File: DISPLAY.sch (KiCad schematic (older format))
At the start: 31 parts, among them Q301 BC849

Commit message: Prepare Display change
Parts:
- removed C310, C311: 100n, Capacitors_SMD:C_0603, symbol C_Small
- removed Q301: BC849, TO_SOT_Packages_SMD:SOT-23, symbol BC849
- removed R301: 4k7, Resistors_SMD:R_0603, symbol R
- removed R302, R303: 0, Resistors_SMD:R_0603, symbol R
- removed R304: 22, Resistors_SMD:R_0603, symbol R
- removed R305, R306, R307, R308, R309: 100, Resistors_SMD:R_0603, symbol R
- removed TP303, TP304, TP305, TP306, TP307, TP308, TP309, TP310, TP311, TP312, TP313, TP314, TP315: TP, buttons:TP, symbol TP
- added P?: SEPS525, symbol CONN_01X35
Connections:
- net labels removed: +3V3, +4V, AO, AO_IN, BL_ON, CS, CS_IN, LED+, LED-, RST, RST_IN, SCK, SCK_IN, SDA, SDA_IN
- wire segments 35 -> 9
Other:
- note added: "160x128 pixel \nOLED display"
- note added: "NC\nVSDH\nVDDH\nVSSH\nIREF\nOSCA2\nOSCA1\nVDDIO\nVSYNCO\nVSYNC\nHSYNC\nDOTCLK\nENABLE\nCPU\nPS\nD17\nD16\nD15\nD14\nD13\nD12\nD11\nD10\nD9\nRS\nCSB\nRDB\nWRB\nRESETB\nVSS\nVDD\nVSSH\nVSDH\nNC"
- note removed: "Constant current: 18mA"
- note removed: "ev.R"
- moved on the sheet: C308, C309, L301, L302, TP301, TP302

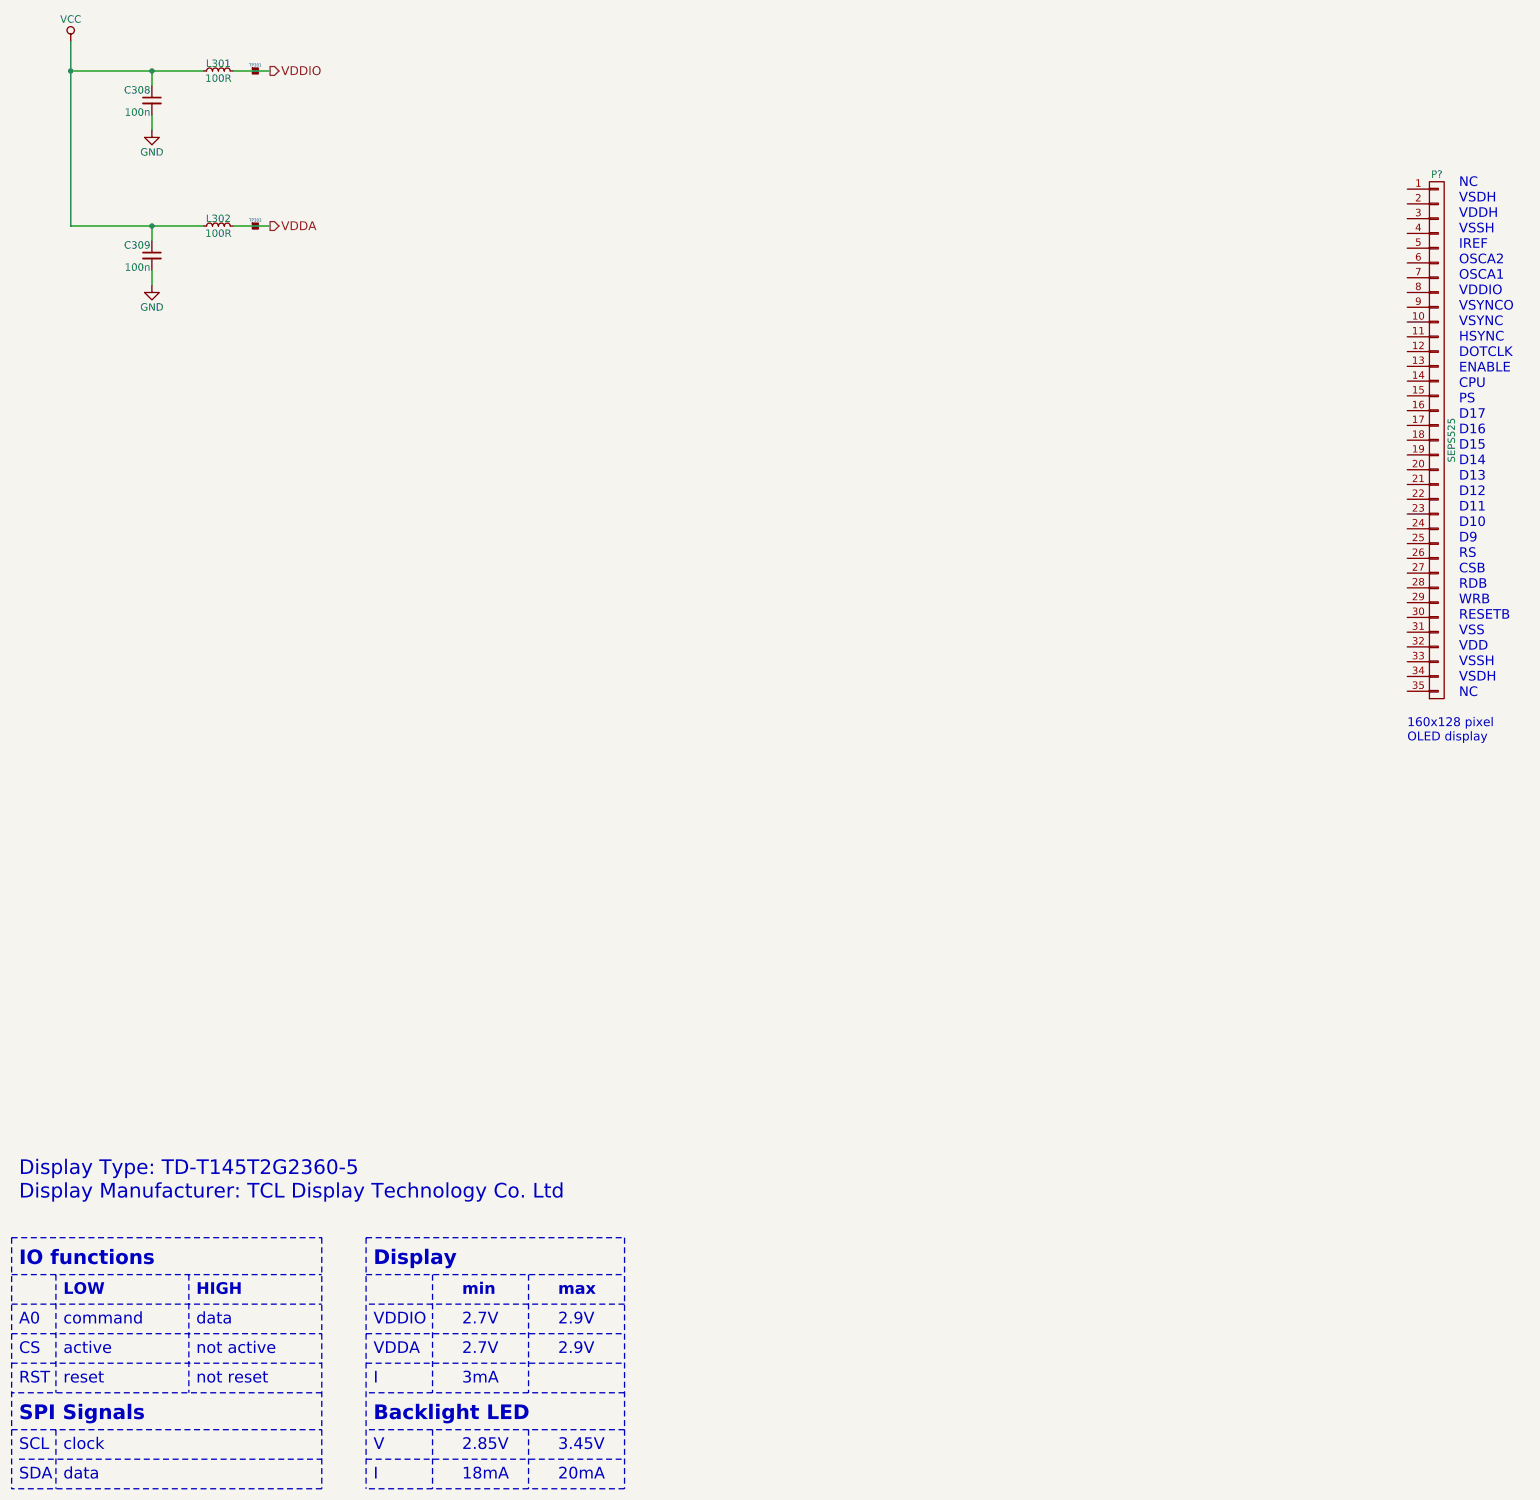
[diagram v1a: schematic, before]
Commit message: Added Interface for OLED display
Added Booster for 4V -> 15V
Added bus for display data
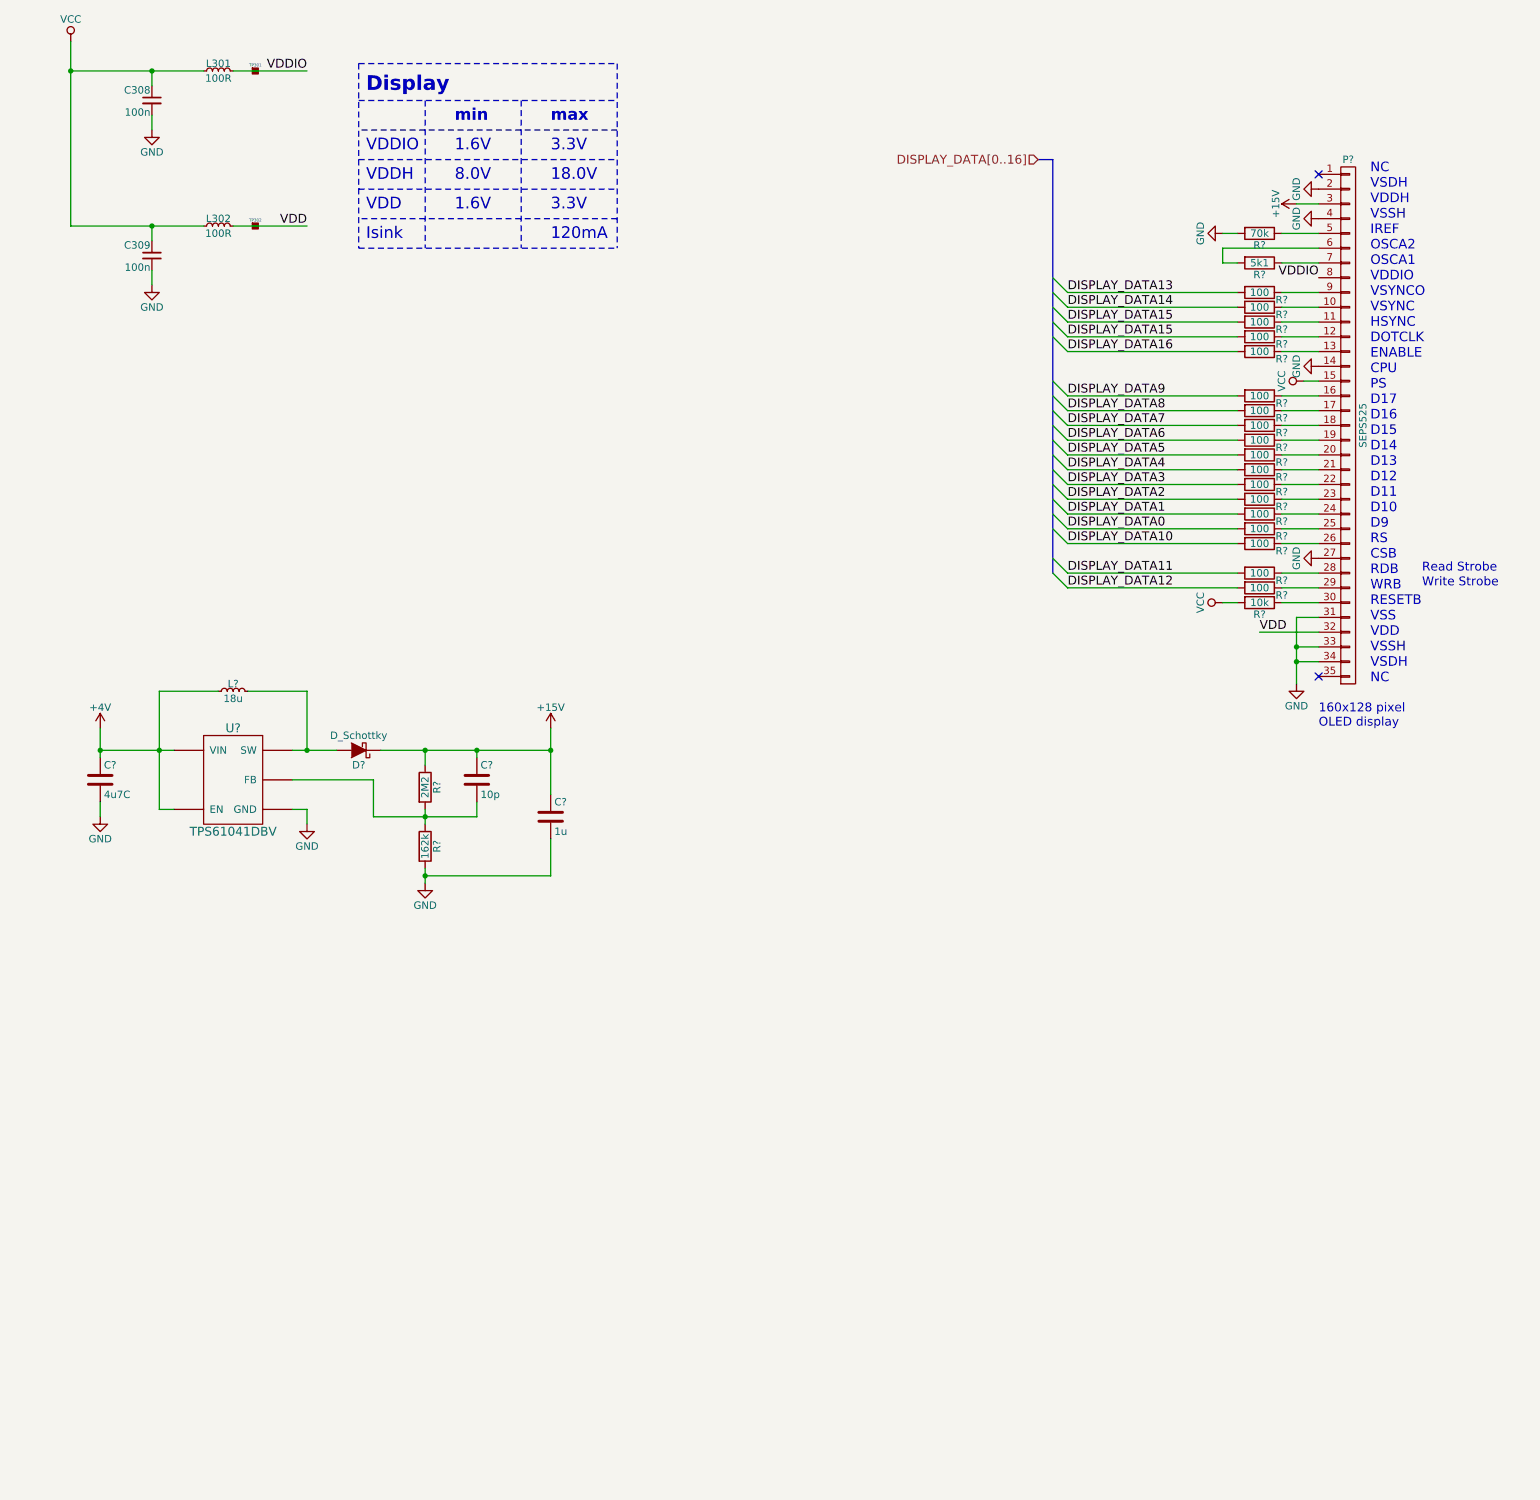
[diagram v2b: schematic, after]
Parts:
- added C?: 4u7C, symbol C
- added C?: 10p, symbol C
- added C?: 1u, symbol C
- added D?: D_Schottky, symbol D_Schottky
- added L?: 18u, Resistors_SMD:R_0603, symbol L_Small
- added R?: 10k, symbol R
- added R?: 5k1, symbol R
- added R?: 70k, symbol R
- added R?: 2M2, symbol R
- added R?: 162k, symbol R
- added R? (x18): 100, symbol R
- added U?: TPS61041DBV, symbol TPS61041DBV
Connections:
- net VDDA is gone; now on net VDD: L302.1
- net GND: now also P?.14 (P14), P?.2 (P2), P?.27 (P27), P?.31 (P31), P?.33 (P33), P?.34 (P34), P?.4 (P4), C?.2, C?.2, R?.2, R?.2, U?.~ (VIN)
- net VCC: now also P?.15 (P15), R?.2
- net VDDIO: now also P?.8 (P8)
- net at P?.10 (P10): now also R?.1
- net at P?.11 (P11): now also R?.1
- net at P?.12 (P12): now also R?.1
- net at P?.13 (P13): now also R?.1
- net at P?.16 (P16): now also R?.1
- net at P?.17 (P17): now also R?.1
- net at P?.18 (P18): now also R?.1
- net at P?.19 (P19): now also R?.1
- net at P?.20 (P20): now also R?.1
- net at P?.21 (P21): now also R?.1
- net at P?.22 (P22): now also R?.1
- net at P?.23 (P23): now also R?.1
- net at P?.24 (P24): now also R?.1
- net at P?.25 (P25): now also R?.1
- net at P?.26 (P26): now also R?.1
- net at P?.28 (P28): now also R?.1
- net at P?.29 (P29): now also R?.1
- net +15V: now reaches P?.3 (P3)
- net +15V: now also C?.1, C?.1, D?.1 (K), R?.1
- net at P?.30 (P30): now also R?.1
- net VDD: now reaches P?.32 (P32)
- net at P?.5 (P5): now also R?.1
- net at P?.6 (P6): now also R?.2
- net at P?.7 (P7): now also R?.1
- net at P?.9 (P9): now also R?.1
- new net: D?.2 (A), L?.1, U?.~ (VIN)
- new net: C?.2, R?.1, R?.2, U?.~ (VIN)
- new net +4V: C?.1, L?.2, U?.~ (VIN)
- new net DISPLAY_DATA0: R?.2
- new net DISPLAY_DATA1: R?.2
- new net DISPLAY_DATA10: R?.2
- new net DISPLAY_DATA11: R?.2
- new net DISPLAY_DATA12: R?.2
- new net DISPLAY_DATA13: R?.2
- new net DISPLAY_DATA14: R?.2
- new net DISPLAY_DATA15: R?.2, R?.2
- new net DISPLAY_DATA16: R?.2
- new net DISPLAY_DATA2: R?.2
- new net DISPLAY_DATA3: R?.2
- new net DISPLAY_DATA4: R?.2
- new net DISPLAY_DATA5: R?.2
- new net DISPLAY_DATA6: R?.2
- new net DISPLAY_DATA7: R?.2
- new net DISPLAY_DATA8: R?.2
- new net DISPLAY_DATA9: R?.2
- no-connect marks 0 -> 2
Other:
- note added: "1.6V"
- note added: "120mA"
- note added: "18.0V"
- note added: "3.3V"
- note added: "8.0V"
- note added: "Isink"
- note added: "Read Strobe"
- note added: "VDD"
- note added: "VDDH"
- note added: "Write Strobe"
- note removed: "18mA"
- note removed: "2.7V"
- note removed: "2.85V"
- note removed: "2.9V"
- note removed: "20mA"
- note removed: "3.45V"
- note removed: "3mA"
- note removed: "A0"
- note removed: "Backlight LED"
- note removed: "CS"
- note removed: "Display Type: TD-T145T2G2360-5\nDisplay Manufacturer: TCL Display Technology Co. Ltd\n"
- note removed: "HIGH"
- note removed: "I"
- note removed: "IO functions"
- note removed: "LOW"
- note removed: "RST"
- note removed: "SCL"
- note removed: "SDA"
- note removed: "SPI Signals"
- note removed: "V"
- note removed: "VDDA"
- note removed: "active"
- note removed: "clock"
- note removed: "command"
- note removed: "data"
- note removed: "not active"
- note removed: "not reset"
- note removed: "reset"
- moved on the sheet: P?

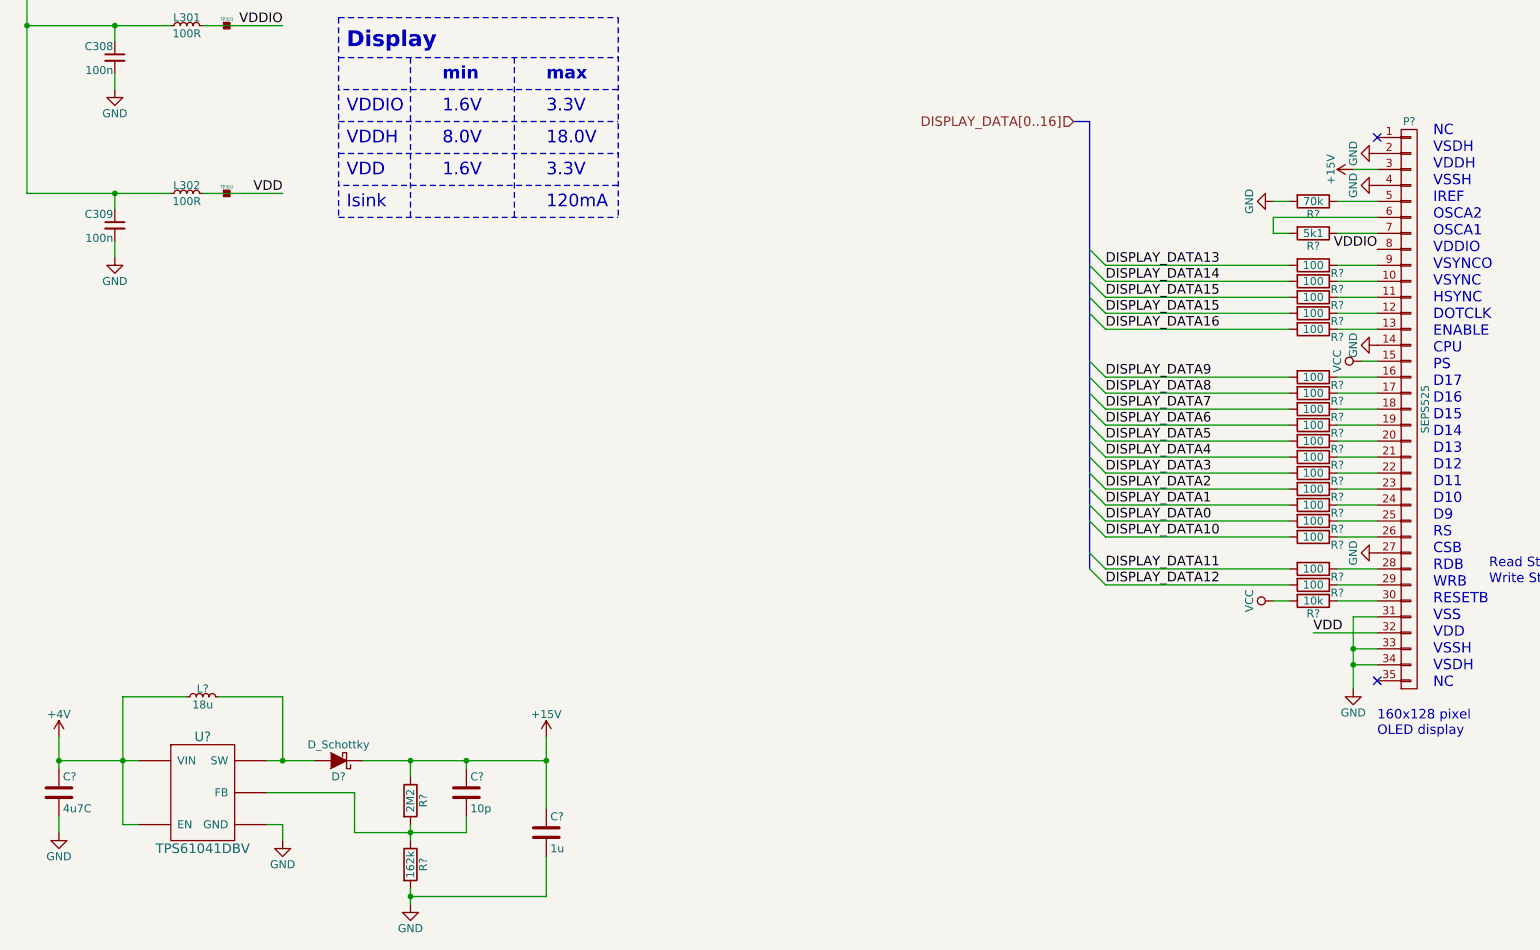
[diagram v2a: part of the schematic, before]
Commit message: Removed WiFi Module added Footprints
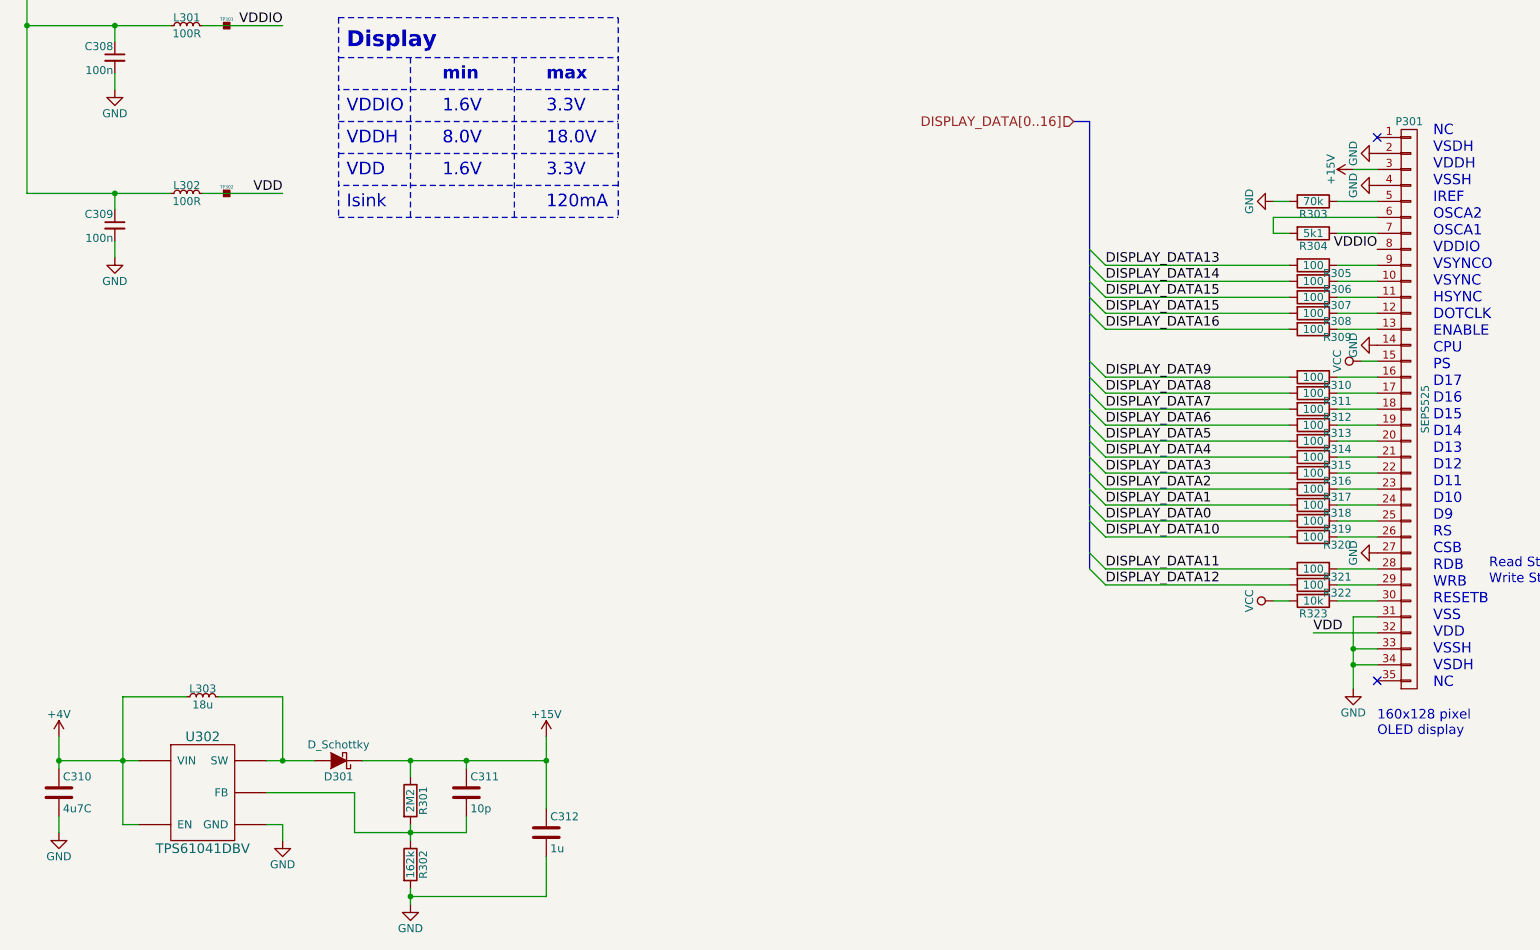
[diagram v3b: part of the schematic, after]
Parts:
- C310, C311, C312: renamed from C?; footprint (none) -> Capacitors_SMD:C_0603
- D301: renamed from D?; footprint (none) -> Diodes_SMD:D_0603
- P301: renamed from P?; footprint (none) -> buttons:FFC-05-35
- R301, R302, R303, R304, R305, R306, R307, R308, R309, R310, R311, R312, R313, R314, R315, R316, R317, R318, R319, R320, R321, R322, R323: renamed from R?; footprint (none) -> Resistors_SMD:R_0603
- U302: renamed from U?; footprint (none) -> TO_SOT_Packages_SMD:SOT-23
- gave numbers to parts that had none: 1

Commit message: started working on implementing i.MX7 core into base schematic
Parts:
- added U?: MCIMX7D7DVM10SC, symbol MCIMX7D7DVM10SC
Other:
- moved on the sheet: C310, C311, C312, D301, L303, P301, R301, R302, R303, R304, R305, R306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
